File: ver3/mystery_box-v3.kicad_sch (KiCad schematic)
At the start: 59 parts, among them J1 Screw_Terminal_01x02, J10 Screw_Terminal_01x02, J11 Screw_Terminal_01x02, J12 Screw_Terminal_01x02, J13 Screw_Terminal_01x02, J14 Screw_Terminal_01x02, J15 Screw_Terminal_01x02, J16 Screw_Terminal_01x02, J17 Screw_Terminal_01x02, J18 Barrel_Jack_MountingPin, J2 XLR3, J20 rj45-CC-X2-Aliexpress, J8 Screw_Terminal_01x02, J9 Screw_Terminal_01x02, M1 24V-Boost-Converter, Q1 IRLZ44N, Q2 IRLZ44N, Q3 IRLZ44N, U1 THVD1400D

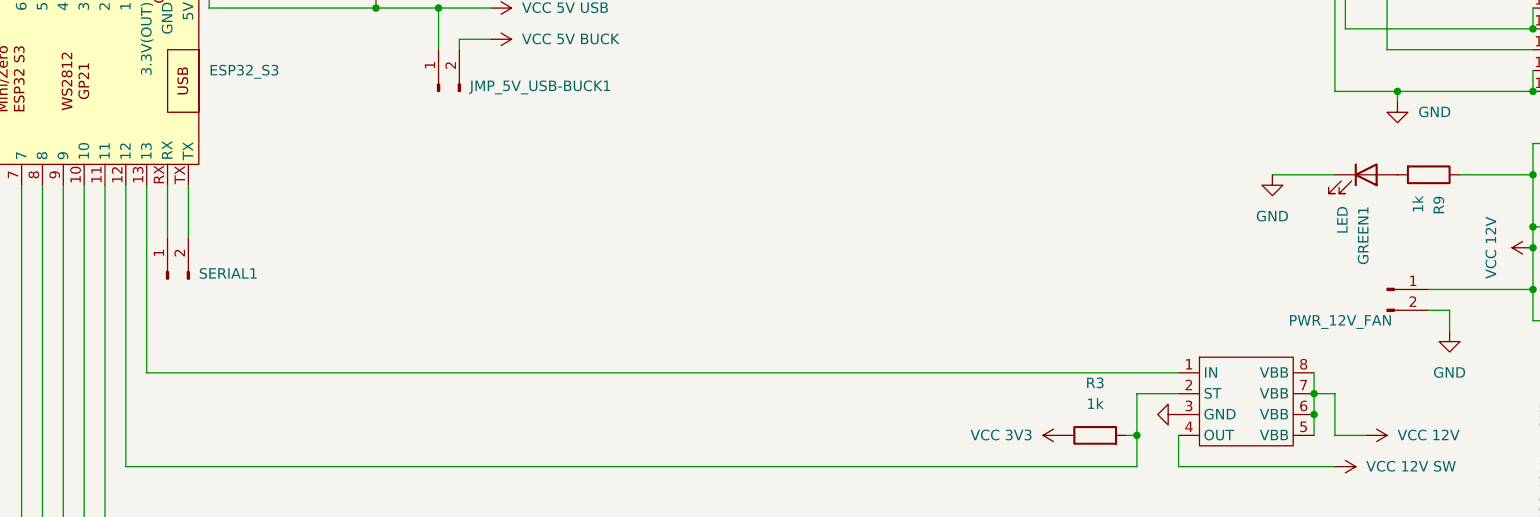
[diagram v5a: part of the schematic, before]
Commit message: ver3: added GND to serial1
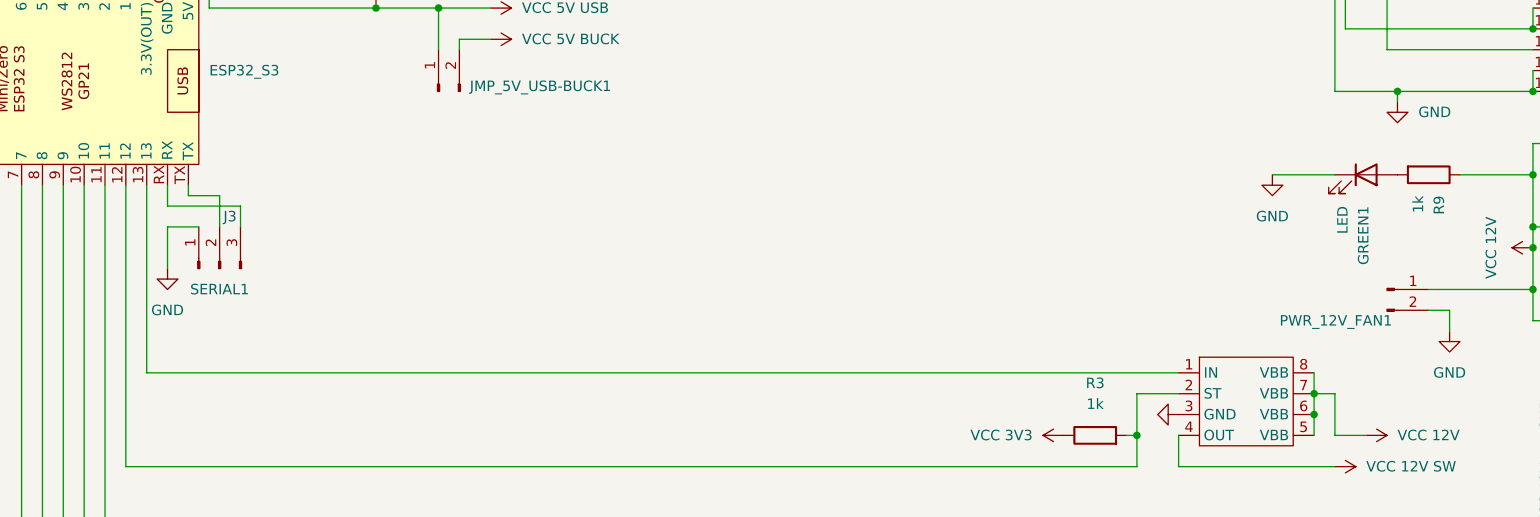
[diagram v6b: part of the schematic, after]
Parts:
- removed SERIAL1: Conn_01x02_Pin, Connector_PinHeader_2.54mm:PinHeader_1x02_P2.54mm_Vertical, symbol Connector:Conn_01x02_Pin
- added J3: SERIAL1, Connector_PinHeader_2.54mm:PinHeader_1x03_P2.54mm_Vertical, symbol Connector:Conn_01x03_Pin
- renumbered PWR_12V_FAN to PWR_12V_FAN1
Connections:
- net GND: now also J3.1 (Pin_1)
- net at ESP32_S3.RX: now also J3.3 (Pin_3)
- net at ESP32_S3.TX: now also J3.2 (Pin_2)
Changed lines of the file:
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@@
 	(wire
 		(pts
+			(xy 97.79 77.47) (xy 106.68 77.47)
+		)
+		(stroke
+			(width 0)
+			(type default)
+		)
+	)
+	(wire
+		(pts
 			(xy 34.29 39.37) (xy 57.15 39.37)
 		)
@@
 	(wire
 		(pts
+			(xy 100.33 74.93) (xy 100.33 76.2)
+		)
+		(stroke
+			(width 0)
+			(type default)
+		)
+	)
+	(wire
+		(pts
 			(xy 240.03 31.75) (xy 240.03 63.5)
 		)
@@
 	(wire
 		(pts
+			(xy 97.79 74.93) (xy 97.79 77.47)
+		)
+		(stroke
+			(width 0)
+			(type default)
+		)
+	)
+	(wire
+		(pts
 			(xy 19.05 63.5) (xy 26.67 63.5)
 		)
@@
 	(wire
 		(pts
-			(xy 100.33 81.28) (xy 100.33 74.93)
-		)
-		(stroke
-			(width 0)
-			(type default)
-		)
-	)
-	(wire
-		(pts
 			(xy 76.2 171.45) (xy 76.2 180.34)
 		)
@@
 	(wire
 		(pts
+			(xy 97.79 80.01) (xy 97.79 85.09)
+		)
+		(stroke
+			(width 0)
+			(type default)
+		)
+	)
+	(wire
+		(pts
 			(xy 271.78 156.21) (xy 271.78 154.94)
 		)
@@
 	(wire
 		(pts
-			(xy 156.21 35.56) (xy 166.37 35.56)
+			(xy 104.14 76.2) (xy 104.14 80.01)
 		)
 		(stroke
@@
 	(wire
 		(pts
-			(xy 274.32 18.415) (xy 274.32 19.05)
+			(xy 156.21 35.56) (xy 166.37 35.56)
 		)
 		(stroke
@@
 	(wire
 		(pts
-			(xy 204.47 31.75) (xy 200.66 31.75)
+			(xy 274.32 18.415) (xy 274.32 19.05)
 		)
 		(stroke
@@
 	(wire
 		(pts
-			(xy 97.79 81.28) (xy 97.79 74.93)
+			(xy 204.47 31.75) (xy 200.66 31.75)
 		)
 		(stroke
@@
 	(wire
 		(pts
+			(xy 100.33 76.2) (xy 104.14 76.2)
+		)
+		(stroke
+			(width 0)
+			(type default)
+		)
+	)
+	(wire
+		(pts
 			(xy 26.67 63.5) (xy 26.67 78.74)
 		)
@@
 	(wire
 		(pts
+			(xy 101.6 80.01) (xy 97.79 80.01)
+		)
+		(stroke
+			(width 0)
+			(type default)
+		)
+	)
+	(wire
+		(pts
 			(xy 66.04 71.12) (xy 58.42 71.12)
 		)
@@
 	(wire
 		(pts
+			(xy 106.68 77.47) (xy 106.68 80.01)
+		)
+		(stroke
+			(width 0)
+			(type default)
+		)
+	)
+	(wire
+		(pts
 			(xy 91.44 24.13) (xy 91.44 33.02)
 		)
@@
 	(symbol
 		(lib_id "power:GND")
+		(at 97.79 85.09 0)
+		(unit 1)
+		(exclude_from_sim no)
+		(in_bom yes)
+		(on_board yes)
+		(dnp no)
+		(fields_autoplaced yes)
+		(property "Reference" "#PWR061"
+			(at 97.79 91.44 0)
+			(effects
+				(font
+					(size 1.27 1.27)
+				)
+				(hide yes)
+			)
+		)
+		(property "Value" "GND"
+			(at 97.79 90.17 0)
+			(effects
+				(font
+					(size 1.27 1.27)
+				)
+			)
+		)
+		(property "Footprint" ""
+			(at 97.79 85.09 0)
+			(effects
+				(font
+					(size 1.27 1.27)
+				)
+				(hide yes)
+			)
+		)
+		(property "Datasheet" ""
+			(at 97.79 85.09 0)
+			(effects
+				(font
+					(size 1.27 1.27)
+				)
+				(hide yes)
+			)
+		)
+		(property "Description" "Power symbol creates a global label with name \"GND\" , ground"
+			(at 97.79 85.09 0)
+			(effects
+				(font
+					(size 1.27 1.27)
+				)
+				(hide yes)
+			)
+		)
+		(pin "1"
+		)
+		(instances
+			(project ""
+				(path "/cbbaaa27-ed93-4129-abc1-94959947e6fe"
+					(reference "#PWR061")
+					(unit 1)
+				)
+			)
+		)
+	)
+	(symbol
+		(lib_id "power:GND")
 		(at 168.91 24.13 0)
 		(unit 1)
@@
 	)
 	(symbol
+		(lib_id "Connector:Conn_01x03_Pin")
+		(at 104.14 85.09 90)
+		(unit 1)
+		(exclude_from_sim no)
+		(in_bom yes)
+		(on_board yes)
+		(dnp no)
+		(property "Reference" "J3"
+			(at 105.41 78.74 90)
+			(effects
+				(font
+					(size 1.27 1.27)
+				)
+			)
+		)
+		(property "Value" "SERIAL1"
+			(at 104.14 87.63 90)
+			(effects
+				(font
+					(size 1.27 1.27)
+				)
+			)
+		)
+		(property "Footprint" "Connector_PinHeader_2.54mm:PinHeader_1x03_P2.54mm_Vertical"
+			(at 104.14 85.09 0)
+			(effects
+				(font
+					(size 1.27 1.27)
+				)
+				(hide yes)
+			)
+		)
+		(property "Datasheet" "~"
+			(at 104.14 85.09 0)
+			(effects
+				(font
+					(size 1.27 1.27)
+				)
+				(hide yes)
+			)
+		)
+		(property "Description" "Generic connector, single row, 01x03, script generated"
+			(at 104.14 85.09 0)
+			(effects
+				(font
+					(size 1.27 1.27)
+				)
+				(hide yes)
+			)
+		)
+		(pin "3"
+		)
+		(pin "2"
+		)
+		(pin "1"
+		)
+		(instances
+			(project ""
+				(path "/cbbaaa27-ed93-4129-abc1-94959947e6fe"
+					(reference "J3")
+					(unit 1)
+				)
+			)
+		)
+	)
+	(symbol
 		(lib_id "power:VCC")
 		(at 168.91 35.56 270)
@@
 		(on_board yes)
 		(dnp no)
-		(property "Reference" "PWR_12V_FAN"
+		(property "Reference" "PWR_12V_FAN1"
 			(at 247.0151 91.44 0)
 			(effects
@@
 			(project "mystery_box-v3"
 				(path "/cbbaaa27-ed93-4129-abc1-94959947e6fe"
-					(reference "PWR_12V_FAN")
+					(reference "PWR_12V_FAN1")
 					(unit 1)
 				)
@@
 					(unit 1)
 				)
-			)
-		)
-	)
-	(symbol
-		(lib_id "Connector:Conn_01x02_Pin")
-		(at 97.79 86.36 90)
-		(unit 1)
-		(exclude_from_sim no)
-		(in_bom yes)
-		(on_board yes)
-		(dnp no)
-		(fields_autoplaced yes)
-		(property "Reference" "SERIAL1"
-			(at 101.6 85.7249 90)
-			(effects
-				(font
-					(size 1.27 1.27)
-				)
-				(justify right)
-			)
-		)
-		(property "Value" "Conn_01x02_Pin"
-			(at 101.6 86.9949 90)
-			(effects
-				(font
-					(size 1.27 1.27)
-				)
-				(justify right)
-				(hide yes)
-			)
-		)
-		(property "Footprint" "Connector_PinHeader_2.54mm:PinHeader_1x02_P2.54mm_Vertical"
-			(at 97.79 86.36 0)
-			(effects
-				(font
-					(size 1.27 1.27)
-				)
-				(hide yes)
-			)
-		)
-		(property "Datasheet" "~"
-			(at 97.79 86.36 0)
-			(effects
-				(font
-					(size 1.27 1.27)
-				)
-				(hide yes)
-			)
-		)
-		(property "Description" "Generic connector, single row, 01x02, script generated"
-			(at 97.79 86.36 0)
-			(effects
-				(font
-					(size 1.27 1.27)
-				)
-				(hide yes)
-			)
-		)
-		(pin "2"
-		)
-		(pin "1"
-		)
-		(instances
-			(project "mystery_box-v3"
-				(path "/cbbaaa27-ed93-4129-abc1-94959947e6fe"
-					(reference "SERIAL1")
-					(unit 1)
-				)

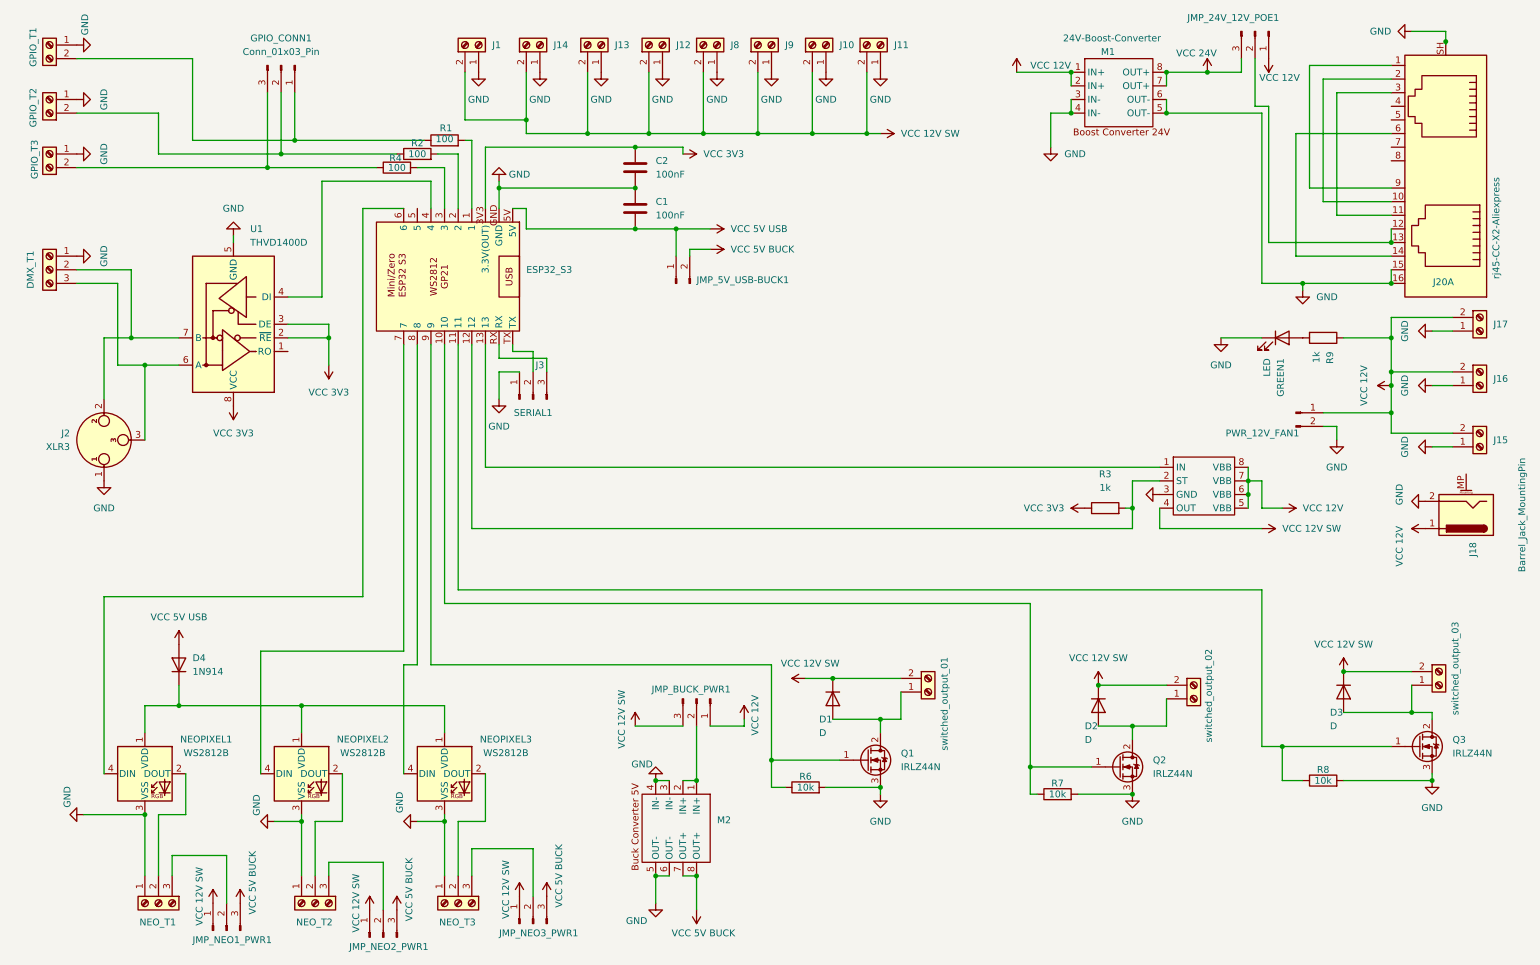
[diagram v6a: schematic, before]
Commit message: ver3: silkscreen beaty & 12v fused LED
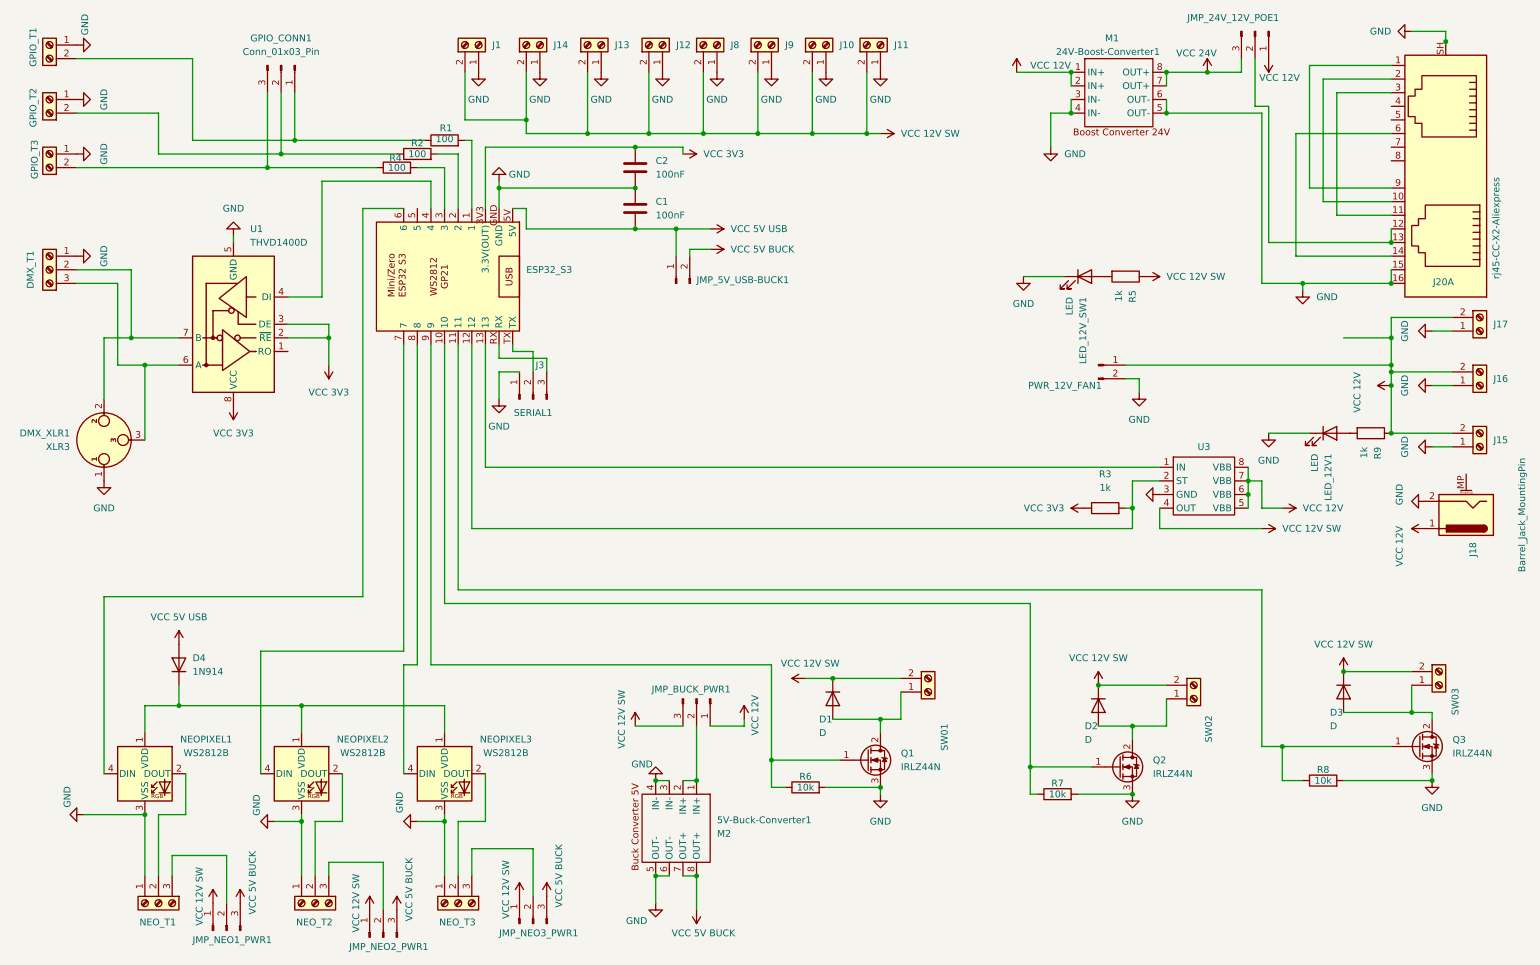
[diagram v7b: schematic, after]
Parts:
- added LED_12V_SW1: LED, LED_THT:LED_D3.0mm_Horizontal_O1.27mm_Z2.0mm_Clear, symbol Device:LED
- added R5: 1k, Resistor_THT:R_Axial_DIN0207_L6.3mm_D2.5mm_P10.16mm_Horizontal, symbol Device:R
- 24V-Boost-Converter1: renamed from M1; value 24V-Boost-Converter -> M1
- 5V-Buck-Converter1: renamed from M2; value ~ -> M2
- SmartSwitch1: renamed from U3; value ~ -> U3
- renumbered J2 to DMX_XLR1, GREEN1 to LED_12V1, switched_output_01 to SW01, switched_output_02 to SW02, switched_output_03 to SW03
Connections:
- net GND: now also LED_12V_SW1.1 (K)
- net VCC 12V SW: now also R5.1
- new net: LED_12V_SW1.2 (A), R5.2
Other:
- moved on the sheet: LED_12V1, PWR_12V_FAN1, R9
